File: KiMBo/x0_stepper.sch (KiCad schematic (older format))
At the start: 25 parts, among them U19 TMC2130

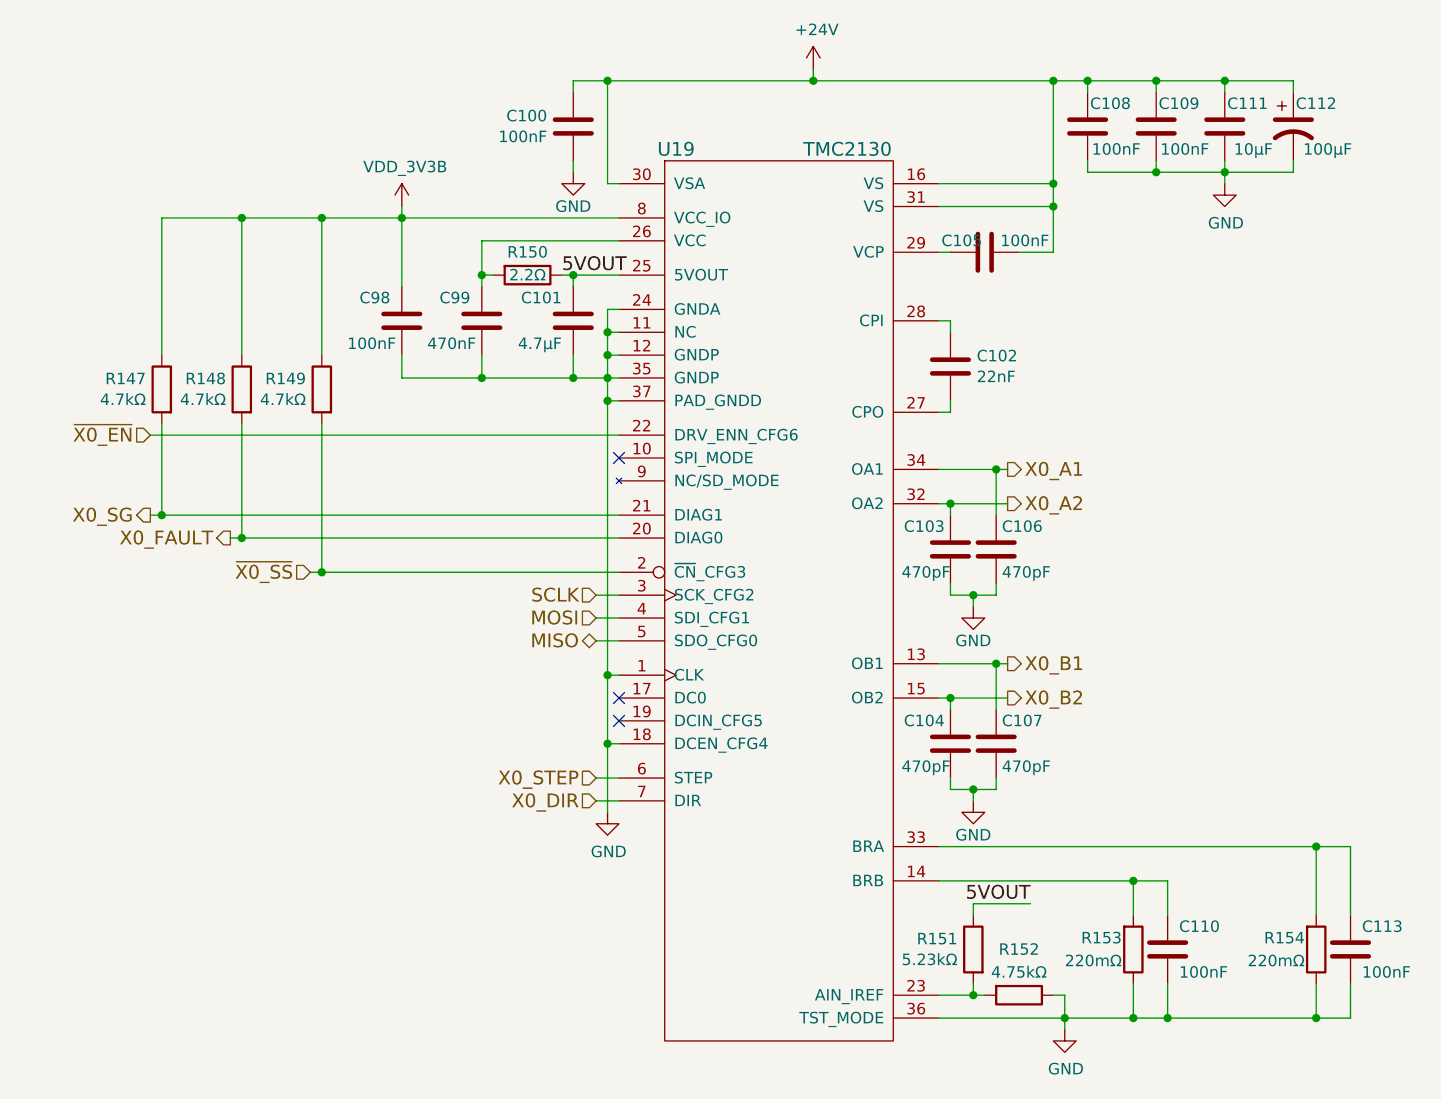
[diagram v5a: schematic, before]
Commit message: Begin layout
Arrange all connectors to get a feel for the area.
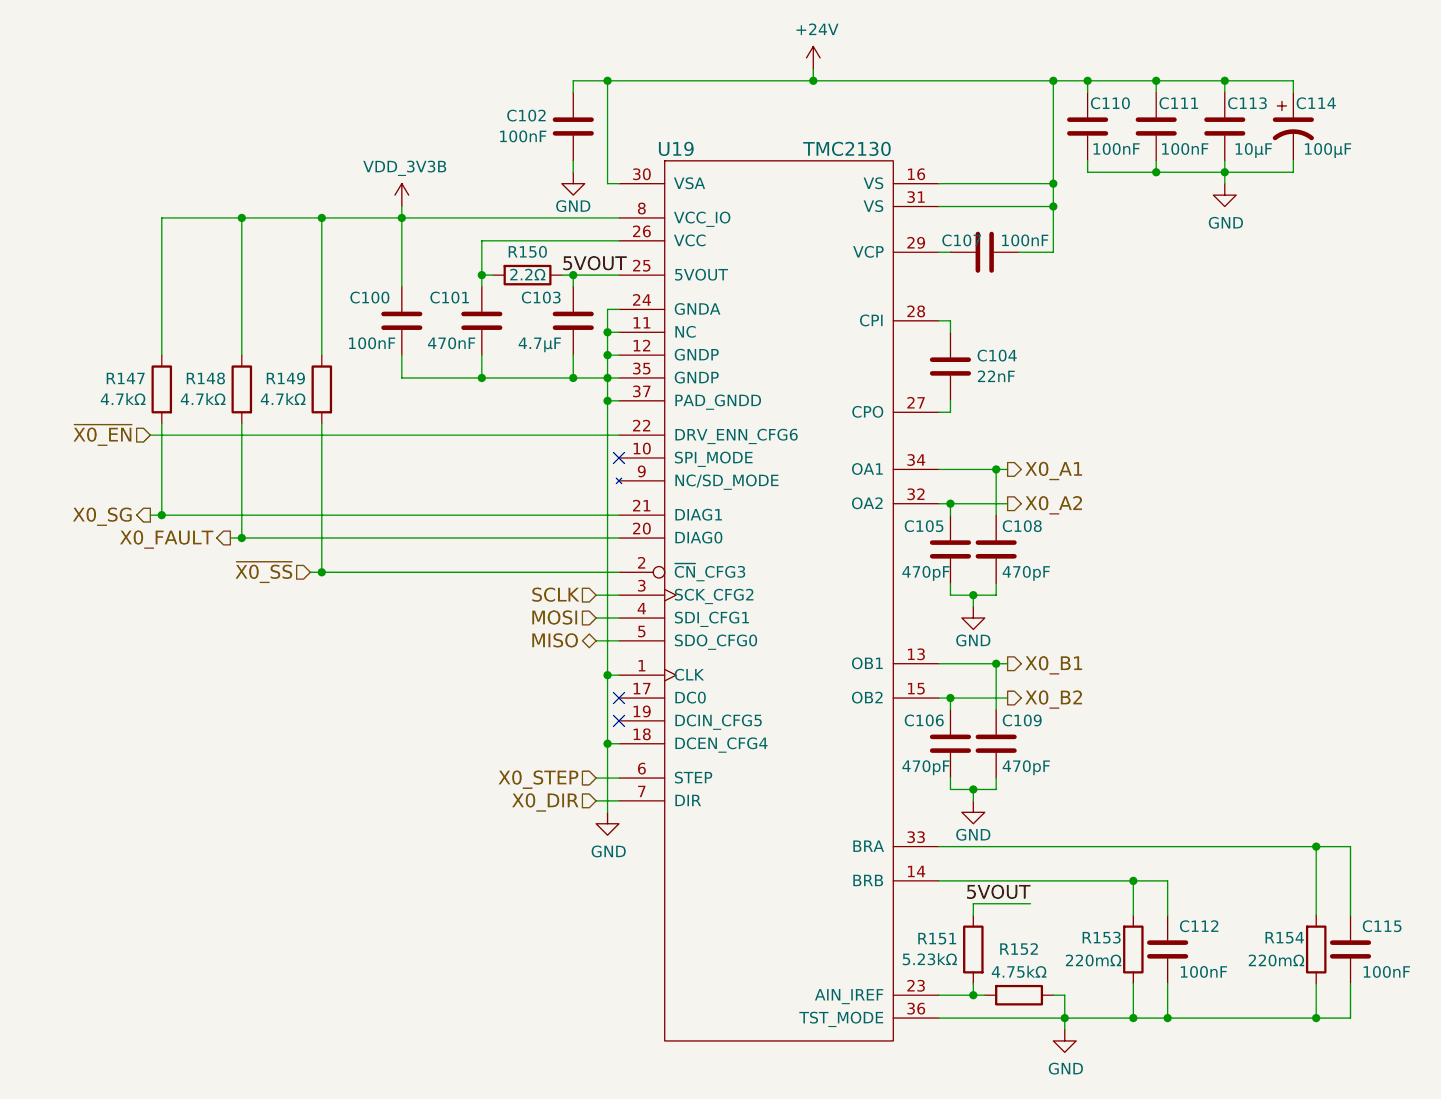
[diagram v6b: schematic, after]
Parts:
- renumbered C98 to C100, C99 to C101, C100 to C102, C101 to C103, C102 to C104, C103 to C105, C104 to C106, C105 to C107, C106 to C108, C107 to C109, C108 to C110, C109 to C111, C110 to C112, C111 to C113, C112 to C114, C113 to C115
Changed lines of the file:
@@
 X0_SG
 $Comp
-L C C100
+L C C102
 U 1 1 5BA7E13B
 P 7500 3100
-F 0 "C100" H 7386 3054 50  0000 R CNN
+F 0 "C102" H 7386 3054 50  0000 R CNN
 F 1 "100nF" H 7386 3145 50  0000 R CNN
 F 2 "Capacitors_SMD:C_0603" H 7538 2950 50  0001 C CNN
@@
 $EndComp
 $Comp
-L C C105
+L C C107
 U 1 1 5BA7E13C
 P 9300 3650
-F 0 "C105" V 9250 3550 50  0000 C CNN
+F 0 "C107" V 9250 3550 50  0000 C CNN
 F 1 "100nF" V 9250 3825 50  0000 C CNN
 F 2 "Capacitors_SMD:C_0603" H 9338 3500 50  0001 C CNN
@@
 $EndComp
 $Comp
-L CP1 C112
+L CP1 C114
 U 1 1 58C092C4
 P 10650 3100
-F 0 "C112" H 10750 3200 50  0000 C CNN
+F 0 "C114" H 10750 3200 50  0000 C CNN
 F 1 "100μF" H 10800 3000 50  0000 C CNN
 F 2 "Capacitors_SMD:c_elec_8x10" H 10650 3100 50  0001 C CNN
@@
 $EndComp
 $Comp
-L C C108
+L C C110
 U 1 1 58C092CB
 P 9750 3100
-F 0 "C108" H 9650 3200 50  0000 C CNN
+F 0 "C110" H 9650 3200 50  0000 C CNN
 F 1 "100nF" H 9625 3000 50  0000 C CNN
 F 2 "Capacitors_SMD:C_0603" H 9788 2950 50  0001 C CNN
@@
 $EndComp
 $Comp
-L GND #PWR0205
+L GND #PWR0208
 U 1 1 58C092D2
 P 7500 3300
-F 0 "#PWR0205" H 7500 3050 50  0001 C CNN
+F 0 "#PWR0208" H 7500 3050 50  0001 C CNN
 F 1 "GND" H 7500 3150 50  0000 C CNN
 F 2 "" H 7500 3300 50  0000 C CNN
@@
 $EndComp
 $Comp
-L C C109
+L C C111
 U 1 1 5BA7E140
 P 10050 3100
-F 0 "C109" H 9950 3200 50  0000 C CNN
+F 0 "C111" H 9950 3200 50  0000 C CNN
 F 1 "100nF" H 9925 3000 50  0000 C CNN
 F 2 "Capacitors_SMD:C_0603" H 10088 2950 50  0001 C CNN
@@
 $EndComp
 $Comp
-L GND #PWR0206
+L GND #PWR0209
 U 1 1 5BA7E141
 P 10350 3350
-F 0 "#PWR0206" H 10350 3100 50  0001 C CNN
+F 0 "#PWR0209" H 10350 3100 50  0001 C CNN
 F 1 "GND" H 10355 3177 50  0000 C CNN
 F 2 "" H 10350 3350 50  0000 C CNN
@@
 $EndComp
 $Comp
-L +24V #PWR0207
+L +24V #PWR0210
 U 1 1 58C092E5
 P 8550 2850
-F 0 "#PWR0207" H 8550 2700 50  0001 C CNN
+F 0 "#PWR0210" H 8550 2700 50  0001 C CNN
 F 1 "+24V" H 8565 3023 50  0000 C CNN
 F 2 "" H 8550 2850 50  0000 C CNN
@@
 $EndComp
 $Comp
-L C C102
+L C C104
 U 1 1 58C092EB
 P 9150 4150
-F 0 "C102" H 9265 4196 50  0000 L CNN
+F 0 "C104" H 9265 4196 50  0000 L CNN
 F 1 "22nF" H 9265 4105 50  0000 L CNN
 F 2 "Capacitors_SMD:C_0603" H 9188 4000 50  0001 C CNN
@@
 $EndComp
 $Comp
-L GND #PWR0208
+L GND #PWR0211
 U 1 1 5BA7E146
 P 9650 7050
-F 0 "#PWR0208" H 9650 6800 50  0001 C CNN
+F 0 "#PWR0211" H 9650 6800 50  0001 C CNN
 F 1 "GND" H 9655 6877 50  0000 C CNN
 F 2 "" H 9650 7050 50  0000 C CNN
@@
 $EndComp
 $Comp
-L C C99
+L C C101
 U 1 1 5BA7E148
 P 7100 3950
-F 0 "C99" H 7150 4050 50  0000 L CNN
+F 0 "C101" H 7150 4050 50  0000 L CNN
 F 1 "470nF" H 7125 3850 50  0000 L CNN
 F 2 "Capacitors_SMD:C_0603" H 7138 3800 50  0001 C CNN
@@
 NoConn ~ 7700 5700
 $Comp
-L GND #PWR0209
+L GND #PWR0212
 U 1 1 5BA7E149
 P 7650 6100
-F 0 "#PWR0209" H 7650 5850 50  0001 C CNN
+F 0 "#PWR0212" H 7650 5850 50  0001 C CNN
 F 1 "GND" H 7655 5927 50  0000 C CNN
 F 2 "" H 7650 6100 50  0000 C CNN
@@
 $EndComp
 $Comp
-L C C110
+L C C112
 U 1 1 5BA7E14A
 P 10100 6700
-F 0 "C110" H 10150 6800 50  0000 L CNN
+F 0 "C112" H 10150 6800 50  0000 L CNN
 F 1 "100nF" H 10150 6600 50  0000 L CNN
 F 2 "Capacitors_SMD:C_0603" H 10138 6550 50  0001 C CNN
@@
 NoConn ~ 7700 4550
 $Comp
-L C C101
+L C C103
 U 1 1 5BA7E14C
 P 7500 3950
-F 0 "C101" H 7550 4050 50  0000 L CNN
+F 0 "C103" H 7550 4050 50  0000 L CNN
 F 1 "4.7μF" H 7550 3850 50  0000 L CNN
 F 2 "Capacitors_SMD:C_0603" H 7538 3800 50  0001 C CNN
@@
 $EndComp
 $Comp
-L C C113
+L C C115
 U 1 1 58C0935A
 P 10900 6700
-F 0 "C113" H 10950 6800 50  0000 L CNN
+F 0 "C115" H 10950 6800 50  0000 L CNN
 F 1 "100nF" H 10950 6600 50  0000 L CNN
 F 2 "Capacitors_SMD:C_0603" H 10938 6550 50  0001 C CNN
@@
 $EndComp
 $Comp
-L C C103
+L C C105
 U 1 1 58C09363
 P 9150 4950
-F 0 "C103" H 9175 5050 50  0000 L CNN
+F 0 "C105" H 9175 5050 50  0000 L CNN
 F 1 "470pF" H 9150 4850 50  0000 L CNN
 F 2 "Capacitors_SMD:C_0603" H 9188 4800 50  0001 C CNN
@@
 $EndComp
 $Comp
-L GND #PWR0210
+L GND #PWR0213
 U 1 1 58C0936A
 P 9250 5200
-F 0 "#PWR0210" H 9250 4950 50  0001 C CNN
+F 0 "#PWR0213" H 9250 4950 50  0001 C CNN
 F 1 "GND" H 9250 5050 50  0000 C CNN
 F 2 "" H 9250 5200 50  0000 C CNN
@@
 $EndComp
 $Comp
-L C C106
+L C C108
 U 1 1 58C09370
 P 9350 4950
-F 0 "C106" H 9375 5050 50  0000 L CNN
+F 0 "C108" H 9375 5050 50  0000 L CNN
 F 1 "470pF" H 9375 4850 50  0000 L CNN
 F 2 "Capacitors_SMD:C_0603" H 9388 4800 50  0001 C CNN
@@
 $EndComp
 $Comp
-L C C104
+L C C106
 U 1 1 5BA7E154
 P 9150 5800
-F 0 "C104" H 9175 5900 50  0000 L CNN
+F 0 "C106" H 9175 5900 50  0000 L CNN
 F 1 "470pF" H 9150 5700 50  0000 L CNN
 F 2 "Capacitors_SMD:C_0603" H 9188 5650 50  0001 C CNN
@@
 $EndComp
 $Comp
-L GND #PWR0211
+L GND #PWR0214
 U 1 1 58C0937E
 P 9250 6050
-F 0 "#PWR0211" H 9250 5800 50  0001 C CNN
+F 0 "#PWR0214" H 9250 5800 50  0001 C CNN
 F 1 "GND" H 9250 5900 50  0000 C CNN
 F 2 "" H 9250 6050 50  0000 C CNN
@@
 $EndComp
 $Comp
-L C C107
+L C C109
 U 1 1 58C09384
 P 9350 5800
-F 0 "C107" H 9375 5900 50  0000 L CNN
+F 0 "C109" H 9375 5900 50  0000 L CNN
 F 1 "470pF" H 9375 5700 50  0000 L CNN
 F 2 "Capacitors_SMD:C_0603" H 9388 5650 50  0001 C CNN
@@
 Connection ~ 6050 3500
 $Comp
-L C C111
+L C C113
 U 1 1 5BA7E159
 P 10350 3100
-F 0 "C111" H 10250 3200 50  0000 C CNN
+F 0 "C113" H 10250 3200 50  0000 C CNN
 F 1 "10μF" H 10225 3000 50  0000 C CNN
 F 2 "Capacitors_SMD:C_0805" H 10388 2950 50  0001 C CNN
@@
 	5700 3500 7700 3500
 $Comp
-L VDD_3V3B #PWR0212
+L VDD_3V3B #PWR0215
 U 1 1 5A2FF856
 P 6750 3450
-F 0 "#PWR0212" H 6750 3300 50  0001 C CNN
+F 0 "#PWR0215" H 6750 3300 50  0001 C CNN
 F 1 "VDD_3V3B" H 6765 3623 50  0000 C CNN
 F 2 "" H 6750 3450 50  0000 C CNN
@@
 $EndComp
 $Comp
-L C C98
+L C C100
 U 1 1 5A89853C
 P 6750 3950
-F 0 "C98" H 6800 4050 50  0000 L CNN
+F 0 "C100" H 6800 4050 50  0000 L CNN
 F 1 "100nF" H 6775 3850 50  0000 L CNN
 F 2 "Capacitors_SMD:C_0603" H 6788 3800 50  0001 C CNN

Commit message: Arrange connectors and E-stepper circuit
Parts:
- R152: footprint Resistors_SMD:R_0805 -> Resistors_SMD:R_0603
- R154: footprint Resistors_SMD:R_0603 -> Resistors_SMD:R_0805
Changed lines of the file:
@@
 F 0 "R154" H 10700 6650 50  0000 R CNN
 F 1 "220mΩ" H 10700 6750 50  0000 R CNN
-F 2 "Resistors_SMD:R_0603" V 10680 6700 50  0001 C CNN
+F 2 "Resistors_SMD:R_0805" V 10680 6700 50  0001 C CNN
 F 3 "" H 10750 6700 50  0000 C CNN
 	1    10750 6700
@@
 F 0 "R152" V 9250 6900 50  0000 C CNN
 F 1 "4.75kΩ" V 9350 6900 50  0000 C CNN
-F 2 "Resistors_SMD:R_0805" V 9380 6900 50  0001 C CNN
+F 2 "Resistors_SMD:R_0603" V 9380 6900 50  0001 C CNN
 F 3 "" H 9450 6900 50  0000 C CNN
 	1    9450 6900
